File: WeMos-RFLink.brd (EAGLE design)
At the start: 33.2 x 25.7 mm, 13 parts, among them P1 PADSMALL

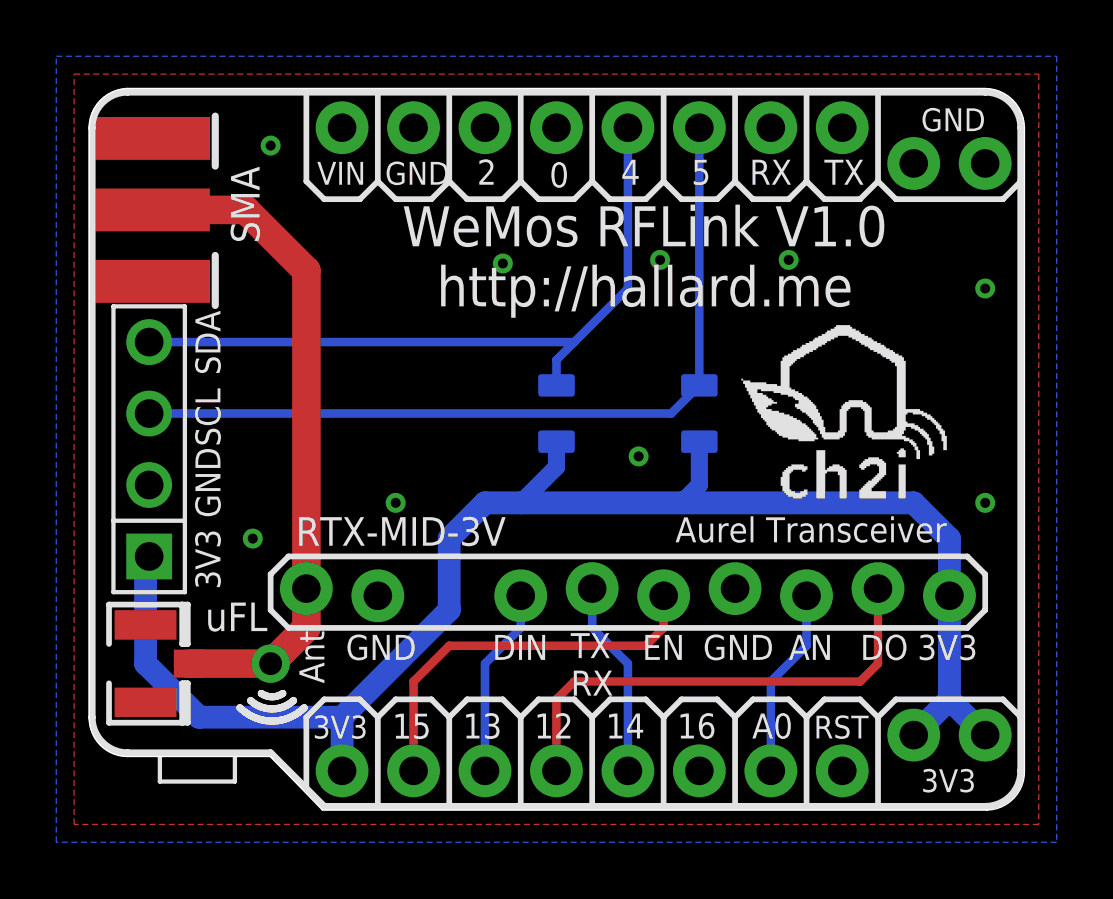
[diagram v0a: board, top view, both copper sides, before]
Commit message: V1.1 Transceiver on bottom shield + RGB LED
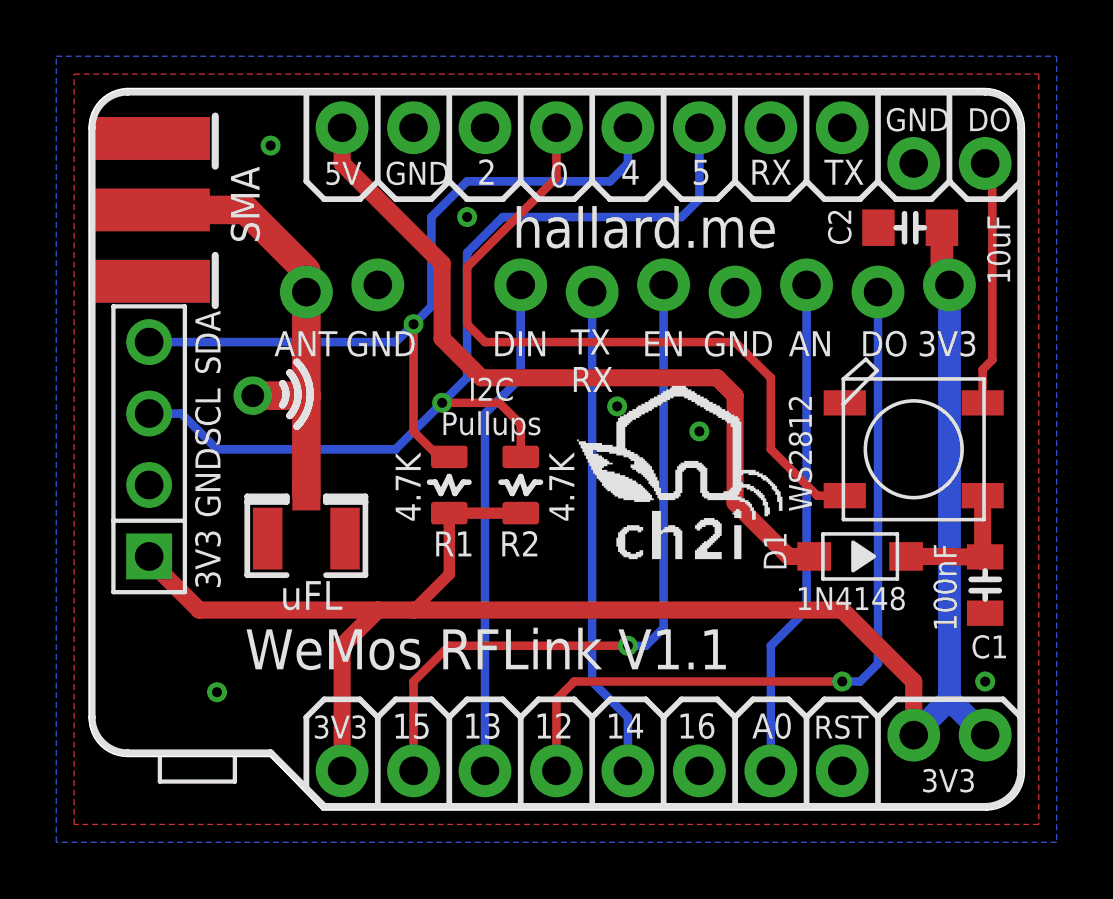
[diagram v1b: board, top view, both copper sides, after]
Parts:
- removed JP4: (no value), SparkFun-Connectors:1X02_NO_SILK
- added C1: 100nF, _c2h:0805-CAP
- added C2: 10uF, _c2h:0805-CAP-LARGEPADS
- added D1: 1N4148, Seeed-Discrete:SOD123-2.7X1.6
- added P2, P3: PADNORMAL, _c2h:PAD
- added WS2812: WS2812B, _c2h:WS2812B
- moved JP3 20.5 mm to (29.2, 2.54), turned to 0 degrees
- moved U$2 12.0 mm to (20.4, 10.8)
- moved AUREL 10.8 mm to (19.1, 18.4), flipped to the bottom, turned to 180 degrees
- moved P1 9.55 mm to (5.71, 14.6)
- moved U-FL 7.24 mm to (7.62, 9.53), turned to 90 degrees
- moved R2 6.84 mm to (15.2, 11.4), flipped to the top
- moved U$1 6.23 mm to (21.3, 10.8)
- moved R1 4.58 mm to (12.7, 11.4), flipped to the top
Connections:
- new net DO: P2.1, WS2812.2
- new net VLED: C1.1, D1.2, WS2812.1
- net 3V3: now also C2.2, JP3.1, JP3.2; no longer JP4.1, JP4.2
- net 5V: now also D1.1
- net GND: now also C1.2, C2.1, P3.1, WS2812.3; no longer JP3.1, JP3.2
- net GPIO0: now also WS2812.4
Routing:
- net 5V: track 0.00 -> 27.6 mm
- net GPIO0: track 0.00 -> 25.7 mm
- net MOSI: track 6.75 -> 17.8 mm
- net A0: track 6.75 -> 17.8 mm
- net SS: track 14.0 -> 25.0 mm, vias 0 -> 1
- net SCK: track 7.00 -> 17.5 mm
- net MISO: track 17.2 -> 27.7 mm, vias 0 -> 1
- net 3V3: track 54.6 -> 64.2 mm
- net DO: track 0.00 -> 8.76 mm
- net ANT: track 23.8 -> 16.3 mm
- net VLED: track 0.00 -> 5.34 mm
- net SCL: track 29.1 -> 33.2 mm, vias 0 -> 1
- net SDA: track 25.3 -> 28.2 mm, vias 0 -> 1
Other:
- board text added: "5V"
- board text added: "ANT"
- board text added: "WeMos RFLink V1.1"
- board text added: "hallard.me"
- board text added: "http://hallard.me"
- board text removed: "Ant"
- board text removed: "VIN"
- board text removed: "WeMos RFLink V1.0 http://hallard.me"
